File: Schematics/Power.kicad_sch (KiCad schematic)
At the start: 12 parts, among them J23 43650-0418, J24 43650-0418, J25 43650-0418, U5 TR05S3V3

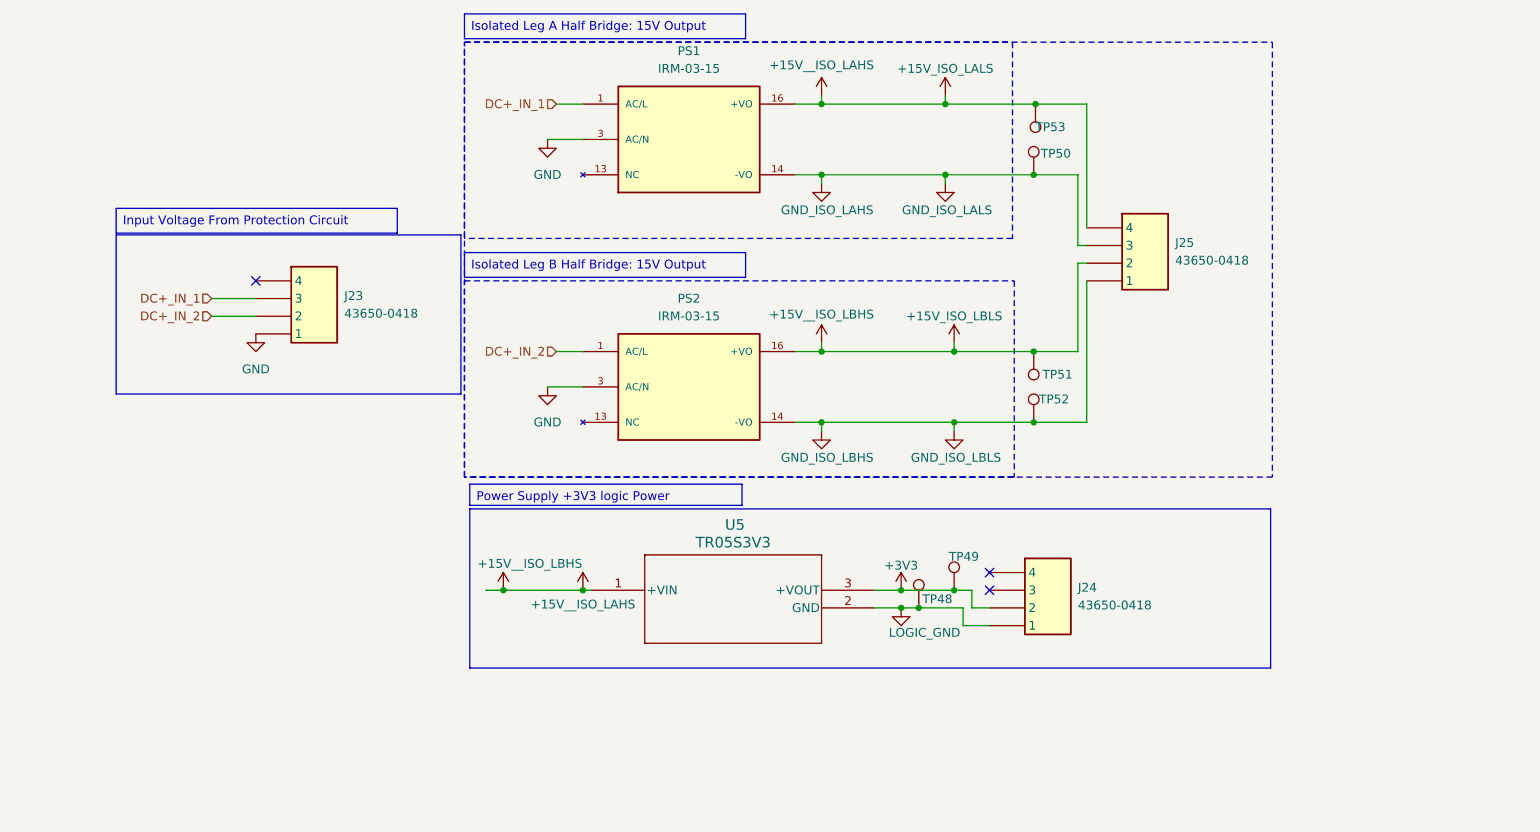
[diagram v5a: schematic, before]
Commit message: [WIP Input Protection Circuit to Controller]
- Added Gate node input protection pin to controller
- Added optocoupler to input protection circuit
- Added 3d model for PC817.....
- Updated PCB to test out PCB modularity
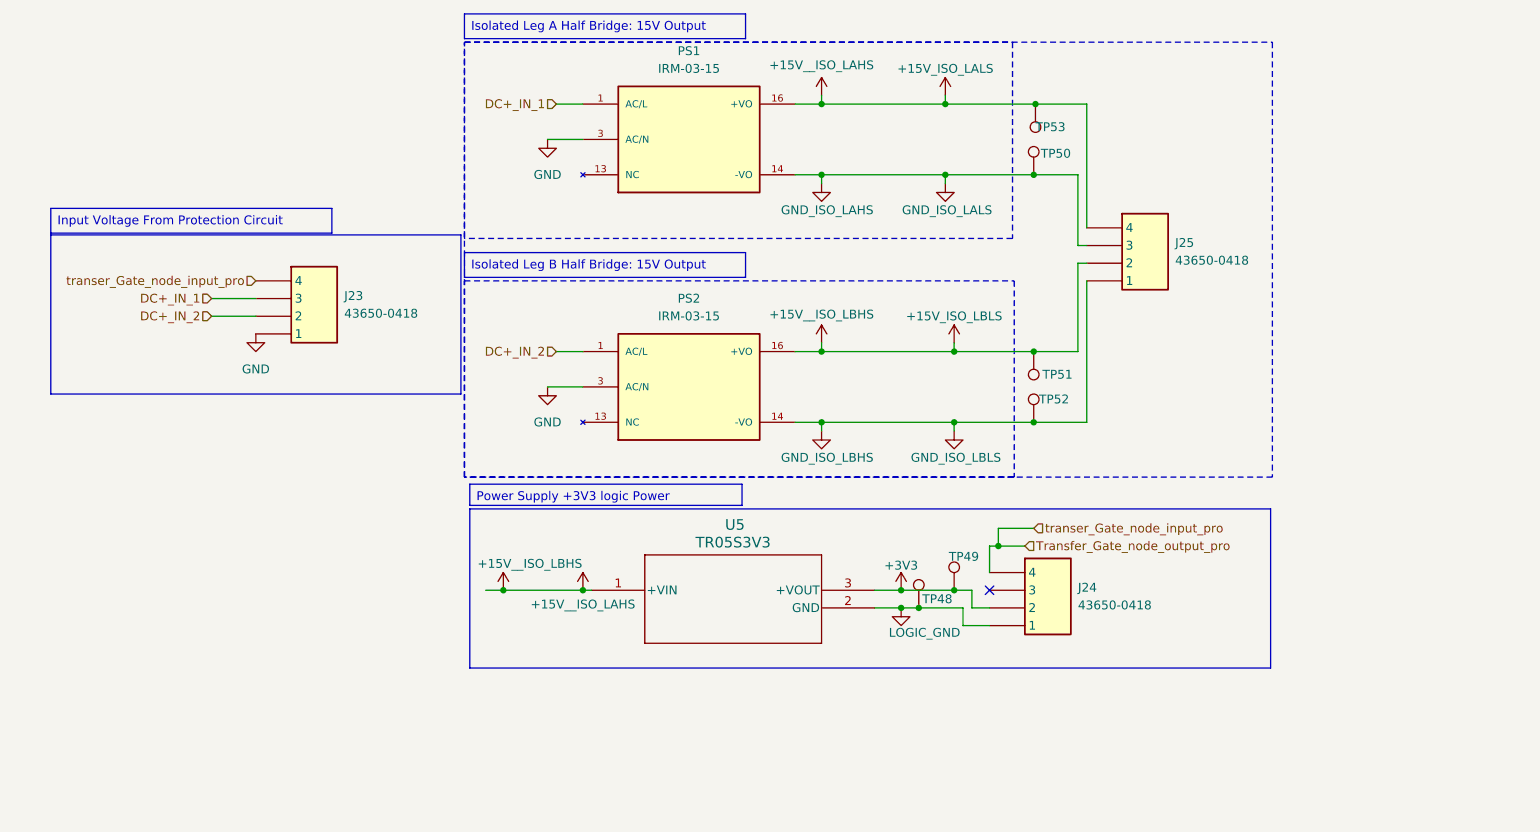
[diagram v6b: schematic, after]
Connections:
- net Transfer_Gate_node_output_pro: now reaches J23.4
- net Transfer_Gate_node_output_pro: now also J24.4
- no-connect marks 3 -> 1
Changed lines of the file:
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@@
 	(paper "A4")
 	(rectangle
-		(start 33.274 77.216)
+		(start 23.876 77.216)
 		(end 82.804 100.076)
 		(stroke
@@
 	(text_box "Input Voltage From Protection Circuit"
 		(exclude_from_sim no)
-		(at 33.274 73.406 0)
+		(at 23.876 73.406 0)
 		(size 40.386 3.556)
 		(margins 0.9525 0.9525 0.9525 0.9525)
@@
 	)
 	(junction
+		(at 160.02 121.92)
+		(diameter 0)
+		(color 0 0 0 0)
+	)
+	(junction
 		(at 153.67 93.98)
 		(diameter 0)
 		(color 0 0 0 0)
-	)
-	(no_connect
-		(at 158.75 125.73)
 	)
 	(no_connect
 		(at 158.75 128.27)
 	)
-	(no_connect
-		(at 53.34 83.82)
+	(wire
+		(pts
+			(xy 165.1 119.38) (xy 160.02 119.38)
+		)
+		(stroke
+			(width 0)
+			(type default)
+		)
 	)
 	(wire
@@
 	(wire
 		(pts
+			(xy 158.75 121.92) (xy 158.75 125.73)
+		)
+		(stroke
+			(width 0)
+			(type default)
+		)
+	)
+	(wire
+		(pts
 			(xy 154.94 130.81) (xy 154.94 133.35)
 		)
@@
 	(wire
 		(pts
+			(xy 163.83 121.92) (xy 160.02 121.92)
+		)
+		(stroke
+			(width 0)
+			(type default)
+		)
+	)
+	(wire
+		(pts
 			(xy 100.33 128.27) (xy 101.6 128.27)
 		)
@@
 	(wire
 		(pts
+			(xy 160.02 119.38) (xy 160.02 121.92)
+		)
+		(stroke
+			(width 0)
+			(type default)
+		)
+	)
+	(wire
+		(pts
 			(xy 134.62 58.42) (xy 130.81 58.42)
 		)
@@
 		(pts
 			(xy 46.99 88.9) (xy 53.34 88.9)
+		)
+		(stroke
+			(width 0)
+			(type default)
+		)
+	)
+	(wire
+		(pts
+			(xy 160.02 121.92) (xy 158.75 121.92)
 		)
 		(stroke
@@
 		)
 	)
+	(hierarchical_label "transer_Gate_node_input_pro"
+		(shape input)
+		(at 165.1 119.38 0)
+		(effects
+			(font
+				(size 1.27 1.27)
+			)
+			(justify left)
+		)
+	)
+	(hierarchical_label "transer_Gate_node_input_pro"
+		(shape input)
+		(at 53.34 83.82 180)
+		(effects
+			(font
+				(size 1.27 1.27)
+			)
+			(justify right)
+		)
+	)
 	(hierarchical_label "DC+_IN_1"
 		(shape input)
@@
 		)
 	)
+	(hierarchical_label "Transfer_Gate_node_output_pro"
+		(shape input)
+		(at 163.83 121.92 0)
+		(effects
+			(font
+				(size 1.27 1.27)
+			)
+			(justify left)
+		)
+	)

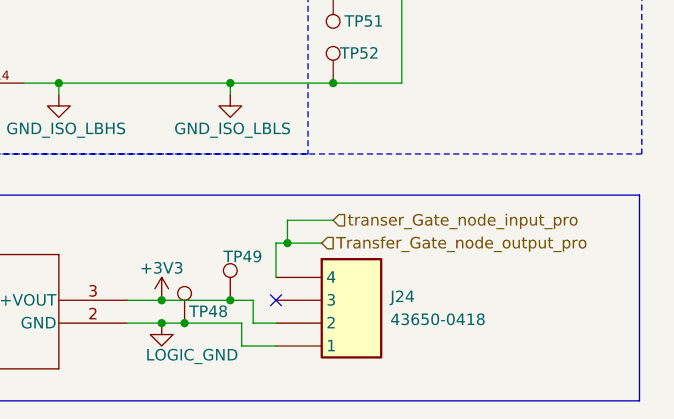
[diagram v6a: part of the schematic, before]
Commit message: Added Precharge Gate Driver to controller and per charge sub circuit
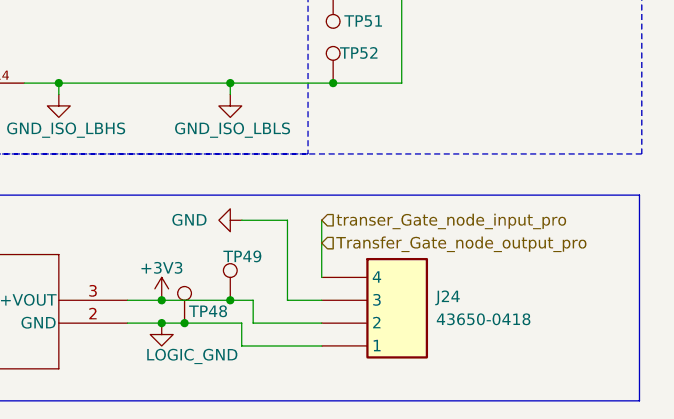
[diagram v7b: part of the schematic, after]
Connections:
- net GND: now also J24.3
- no-connect marks 1 -> 0
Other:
- moved on the sheet: J24
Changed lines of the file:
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@@
-	)
-	(junction
-		(at 160.02 121.92)
-		(diameter 0)
-		(color 0 0 0 0)
 	)
 	(junction
@@
 		(color 0 0 0 0)
 	)
-	(no_connect
-		(at 158.75 128.27)
-	)
-	(wire
-		(pts
-			(xy 165.1 119.38) (xy 160.02 119.38)
-		)
-		(stroke
-			(width 0)
-			(type default)
-		)
-	)
 	(wire
 		(pts
@@
 	(wire
 		(pts
-			(xy 156.21 130.81) (xy 158.75 130.81)
+			(xy 156.21 130.81) (xy 163.83 130.81)
 		)
 		(stroke
@@
 	(wire
 		(pts
-			(xy 158.75 121.92) (xy 158.75 125.73)
+			(xy 163.83 119.38) (xy 163.83 125.73)
 		)
 		(stroke
@@
 	(wire
 		(pts
-			(xy 163.83 121.92) (xy 160.02 121.92)
-		)
-		(stroke
-			(width 0)
-			(type default)
-		)
-	)
-	(wire
-		(pts
 			(xy 100.33 128.27) (xy 101.6 128.27)
 		)
@@
 	(wire
 		(pts
+			(xy 160.02 119.38) (xy 160.02 128.27)
+		)
+		(stroke
+			(width 0)
+			(type default)
+		)
+	)
+	(wire
+		(pts
+			(xy 160.02 128.27) (xy 163.83 128.27)
+		)
+		(stroke
+			(width 0)
+			(type default)
+		)
+	)
+	(wire
+		(pts
 			(xy 134.62 57.15) (xy 134.62 58.42)
 		)
@@
 	(wire
 		(pts
-			(xy 160.02 119.38) (xy 160.02 121.92)
-		)
-		(stroke
-			(width 0)
-			(type default)
-		)
-	)
-	(wire
-		(pts
 			(xy 134.62 58.42) (xy 130.81 58.42)
 		)
@@
 	(wire
 		(pts
-			(xy 154.94 133.35) (xy 158.75 133.35)
+			(xy 154.94 133.35) (xy 163.83 133.35)
 		)
 		(stroke
@@
 	(wire
 		(pts
-			(xy 160.02 121.92) (xy 158.75 121.92)
+			(xy 154.94 119.38) (xy 160.02 119.38)
 		)
 		(stroke
@@
 	(hierarchical_label "transer_Gate_node_input_pro"
 		(shape input)
-		(at 165.1 119.38 0)
+		(at 163.83 119.38 0)
 		(effects
 			(font
@@
 	(symbol
 		(lib_id "SiC_Inverter:43650-0418")
-		(at 158.75 123.19 0)
+		(at 163.83 123.19 0)
 		(unit 1)
 		(exclude_from_sim no)
@@
 		(fields_autoplaced yes)
 		(property "Reference" "J24"
-			(at 171.45 127.8889 0)
+			(at 176.53 127.8889 0)
 			(effects
 				(font
@@
 		)
 		(property "Value" "43650-0418"
-			(at 171.45 130.4289 0)
+			(at 176.53 130.4289 0)
 			(effects
 				(font
@@
 		)
 		(property "Footprint" "SiC_Inverter:436500418"
-			(at 175.26 218.11 0)
+			(at 180.34 218.11 0)
 			(effects
 				(font
@@
 		)
 		(property "Datasheet" "https://www.molex.com/pdm_docs/sd/436500218_sd.pdf"
-			(at 175.26 318.11 0)
+			(at 180.34 318.11 0)
 			(effects
 				(font
@@
 		)
 		(property "Description" "Micro-Fit 3.0 Vertical Header, 3.00mm Pitch, Single Row, 4 Circuits, with PCB Press-fit Metal Retention Clip, Glow-Wire Capable, Black"
-			(at 222.758 141.986 0)
+			(at 227.838 141.986 0)
 			(effects
 				(font
@@
 		)
 		(property "Mouser Part Number" "538-43650-0418"
-			(at 175.26 618.11 0)
+			(at 180.34 618.11 0)
 			(effects
 				(font
@@
 		)
 		(property "Manufacturer_Name" "Molex"
-			(at 175.26 818.11 0)
+			(at 180.34 818.11 0)
 			(effects
 				(font
@@
 		)
 		(property "Manufacturer_Part_Number" "43650-0418"
-			(at 175.26 918.11 0)
+			(at 180.34 918.11 0)
 			(effects
 				(font
@@
 					(unit 1)
 				)
+			)
+		)
+	)
+	(symbol
+		(lib_id "power:GND")
+		(at 154.94 119.38 270)
+		(unit 1)
+		(exclude_from_sim no)
+		(in_bom yes)
+		(on_board yes)
+		(dnp no)
+		(fields_autoplaced yes)
+		(property "Reference" "#PWR0147"
+			(at 148.59 119.38 0)
+			(effects
+				(font
+					(size 1.27 1.27)
+				)
+				(hide yes)
+			)
+		)
+		(property "Value" "GND"
+			(at 151.13 119.3799 90)
+			(effects
+				(font
+					(size 1.27 1.27)
+				)
+				(justify right)
+			)
+		)
+		(property "Footprint" ""
+			(at 154.94 119.38 0)
+			(effects
+				(font
+					(size 1.27 1.27)
+				)
+				(hide yes)
+			)
+		)
+		(property "Datasheet" ""
+			(at 154.94 119.38 0)
+			(effects
+				(font
+					(size 1.27 1.27)
+				)
+				(hide yes)
+			)
+		)
+		(property "Description" "Power symbol creates a global label with name \"GND\" , ground"
+			(at 154.94 119.38 0)
+			(effects
+				(font
+					(size 1.27 1.27)
+				)
+				(hide yes)
+			)
+		)
+		(pin "1"
+		)
+		(instances
+			(project "SiC_Single_Phase_Inverter"
+				(path "/a1ed0539-9735-4ad1-a8fd-87e26e7fce16/e9f9d5ca-7f9f-4dc3-b303-71fca817b963"
+					(reference "#PWR0147")
+					(unit 1)
+				)

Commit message: WIP PCB, Added Test Points, added icon file
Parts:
- renumbered J23 to J25, J24 to J26, J25 to J27, TP48 to TP70, TP49 to TP71, TP53 to TP72, TP50 to TP73, TP51 to TP74, TP52 to TP75
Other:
- moved on the sheet: TP71, TP72, TP74
